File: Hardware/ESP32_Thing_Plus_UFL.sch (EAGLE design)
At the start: 50 parts, among them Q1 2.5A/30V, Q2 MBT3904DW1T1, U1 MCP73831, U3 AP2112K-3.3V, U4 CP210X, U5 ESP-WROOM-3232U-NARROW

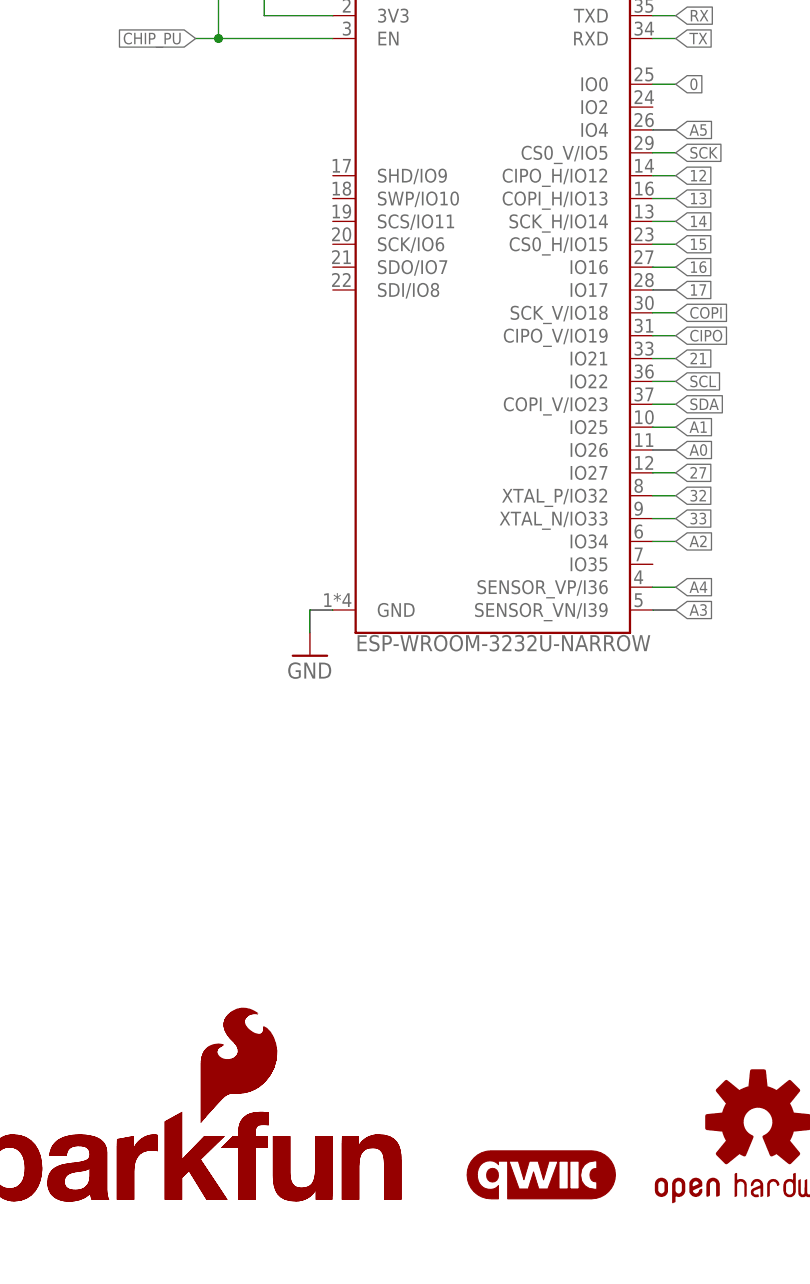
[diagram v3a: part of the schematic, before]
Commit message: aesthetic changes from post review review
-Change CIPO and COPI pin names in symbol to SDI/SDO
-Updated product name bottom silk to include "32"
-Removed extra top silk flame logo at bottom right (since we had room for the full name and flame logo at the top.
-changed silk names for DI/DO to SDI/SDO for more consitency in schematic/board naming.
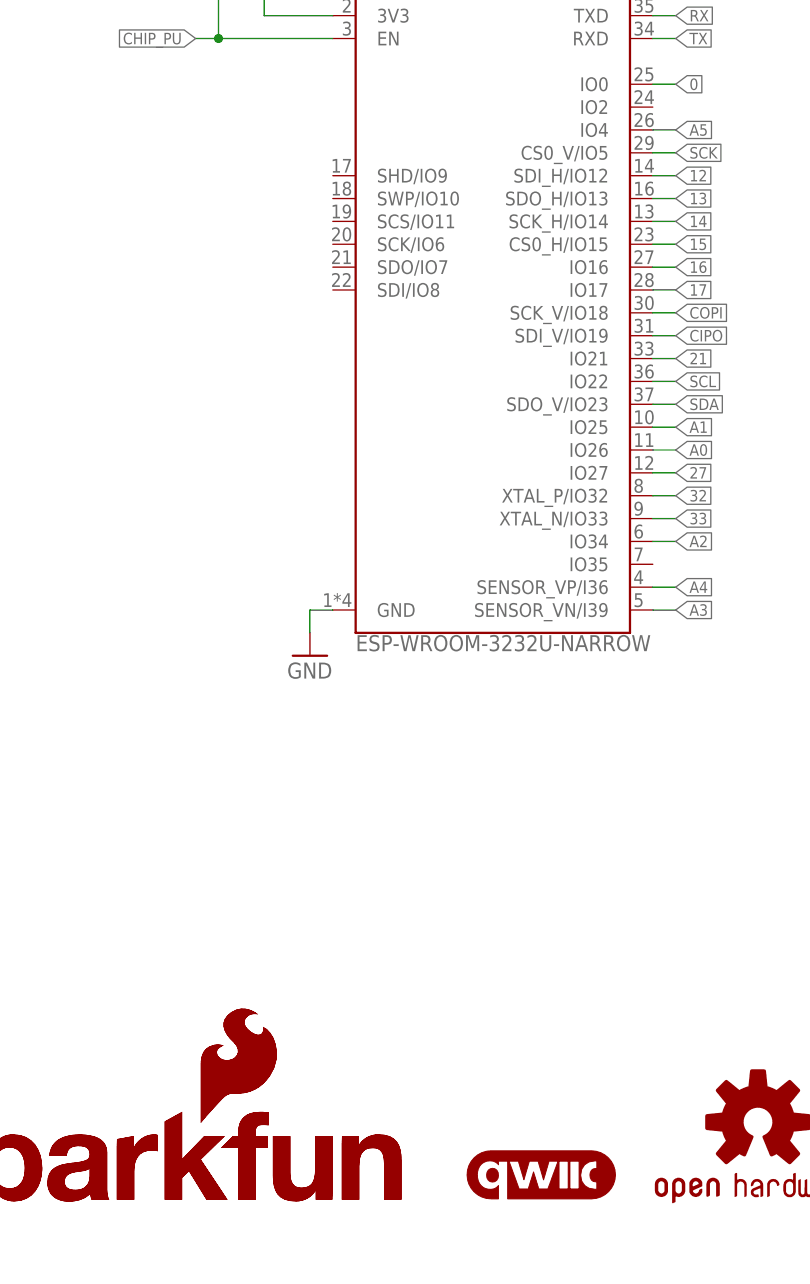
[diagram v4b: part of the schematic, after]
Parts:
- removed LOGO1: SFE_LOGO_FLAME.1_INCH, SparkFun-Aesthetics:SFE_LOGO_FLAME.1_INCH
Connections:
- net 12: now also U5.SDI_H/IO12; no longer U5.CIPO_H/IO12
- net 13: now also U5.SDO_H/IO13; no longer U5.COPI_H/IO13
- net CIPO: now also U5.SDI_V/IO19; no longer U5.CIPO_V/IO19
- net SDA: now also U5.SDO_V/IO23; no longer U5.COPI_V/IO23
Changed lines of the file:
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@@
 <grid distance="0.1" unitdist="inch" unit="inch" style="lines" multiple="1" display="no" altdistance="0.01" altunitdist="inch" altunit="inch"/>
 <layers>
-<layer number="1" name="Top" color="4" fill="1" visible="yes" active="no"/>
-<layer number="2" name="Route2" color="1" fill="3" visible="yes" active="no"/>
-<layer number="3" name="Route3" color="4" fill="3" visible="yes" active="no"/>
-<layer number="4" name="Route4" color="1" fill="4" visible="yes" active="no"/>
-<layer number="5" name="Route5" color="4" fill="4" visible="yes" active="no"/>
-<layer number="6" name="Route6" color="1" fill="8" visible="yes" active="no"/>
-<layer number="7" name="Route7" color="4" fill="8" visible="yes" active="no"/>
-<layer number="8" name="Route8" color="1" fill="2" visible="yes" active="no"/>
-<layer number="9" name="Route9" color="4" fill="2" visible="yes" active="no"/>
-<layer number="10" name="Route10" color="1" fill="7" visible="yes" active="no"/>
-<layer number="11" name="Route11" color="4" fill="7" visible="yes" active="no"/>
-<layer number="12" name="Route12" color="1" fill="5" visible="yes" active="no"/>
-<layer number="13" name="Route13" color="4" fill="5" visible="yes" active="no"/>
-<layer number="14" name="Route14" color="1" fill="6" visible="yes" active="no"/>
-<layer number="15" name="Route15" color="4" fill="6" visible="yes" active="no"/>
-<layer number="16" name="Bottom" color="1" fill="1" visible="yes" active="no"/>
-<layer number="17" name="Pads" color="2" fill="1" visible="yes" active="no"/>
-<layer number="18" name="Vias" color="2" fill="1" visible="yes" active="no"/>
-<layer number="19" name="Unrouted" color="6" fill="1" visible="yes" active="no"/>
-<layer number="20" name="Dimension" color="15" fill="1" visible="yes" active="no"/>
-<layer number="21" name="tPlace" color="16" fill="1" visible="yes" active="no"/>
-<layer number="22" name="bPlace" color="14" fill="1" visible="yes" active="no"/>
-<layer number="23" name="tOrigins" color="15" fill="1" visible="yes" active="no"/>
-<layer number="24" name="bOrigins" color="15" fill="1" visible="yes" active="no"/>
-<layer number="25" name="tNames" color="7" fill="1" visible="yes" active="no"/>
-<layer number="26" name="bNames" color="7" fill="1" visible="yes" active="no"/>
-<layer number="27" name="tValues" color="7" fill="1" visible="yes" active="no"/>
-<layer number="28" name="bValues" color="7" fill="1" visible="yes" active="no"/>
+<layer number="1" name="Top" color="4" fill="1" visible="no" active="no"/>
+<layer number="2" name="Route2" color="1" fill="3" visible="no" active="no"/>
+<layer number="3" name="Route3" color="4" fill="3" visible="no" active="no"/>
+<layer number="4" name="Route4" color="1" fill="4" visible="no" active="no"/>
+<layer number="5" name="Route5" color="4" fill="4" visible="no" active="no"/>
+<layer number="6" name="Route6" color="1" fill="8" visible="no" active="no"/>
+<layer number="7" name="Route7" color="4" fill="8" visible="no" active="no"/>
+<layer number="8" name="Route8" color="1" fill="2" visible="no" active="no"/>
+<layer number="9" name="Route9" color="4" fill="2" visible="no" active="no"/>
+<layer number="10" name="Route10" color="1" fill="7" visible="no" active="no"/>
+<layer number="11" name="Route11" color="4" fill="7" visible="no" active="no"/>
+<layer number="12" name="Route12" color="1" fill="5" visible="no" active="no"/>
+<layer number="13" name="Route13" color="4" fill="5" visible="no" active="no"/>
+<layer number="14" name="Route14" color="1" fill="6" visible="no" active="no"/>
+<layer number="15" name="Route15" color="4" fill="6" visible="no" active="no"/>
+<layer number="16" name="Bottom" color="1" fill="1" visible="no" active="no"/>
+<layer number="17" name="Pads" color="2" fill="1" visible="no" active="no"/>
+<layer number="18" name="Vias" color="2" fill="1" visible="no" active="no"/>
+<layer number="19" name="Unrouted" color="6" fill="1" visible="no" active="no"/>
+<layer number="20" name="Dimension" color="15" fill="1" visible="no" active="no"/>
+<layer number="21" name="tPlace" color="16" fill="1" visible="no" active="no"/>
+<layer number="22" name="bPlace" color="14" fill="1" visible="no" active="no"/>
+<layer number="23" name="tOrigins" color="15" fill="1" visible="no" active="no"/>
+<layer number="24" name="bOrigins" color="15" fill="1" visible="no" active="no"/>
+<layer number="25" name="tNames" color="7" fill="1" visible="no" active="no"/>
+<layer number="26" name="bNames" color="7" fill="1" visible="no" active="no"/>
+<layer number="27" name="tValues" color="7" fill="1" visible="no" active="no"/>
+<layer number="28" name="bValues" color="7" fill="1" visible="no" active="no"/>
 <layer number="29" name="tStop" color="7" fill="3" visible="no" active="no"/>
 <layer number="30" name="bStop" color="7" fill="6" visible="no" active="no"/>
@@
 <layer number="35" name="tGlue" color="7" fill="4" visible="no" active="no"/>
 <layer number="36" name="bGlue" color="7" fill="5" visible="no" active="no"/>
-<layer number="37" name="tTest" color="7" fill="1" visible="yes" active="no"/>
-<layer number="38" name="bTest" color="7" fill="1" visible="yes" active="no"/>
+<layer number="37" name="tTest" color="7" fill="1" visible="no" active="no"/>
+<layer number="38" name="bTest" color="7" fill="1" visible="no" active="no"/>
 <layer number="39" name="tKeepout" color="4" fill="11" visible="no" active="no"/>
 <layer number="40" name="bKeepout" color="1" fill="11" visible="no" active="no"/>
@@
 <layer number="44" name="Drills" color="7" fill="1" visible="no" active="no"/>
 <layer number="45" name="Holes" color="7" fill="1" visible="no" active="no"/>
-<layer number="46" name="Milling" color="3" fill="1" visible="yes" active="no"/>
-<layer number="47" name="Measures" color="7" fill="1" visible="yes" active="no"/>
-<layer number="48" name="Document" color="7" fill="1" visible="yes" active="no"/>
-<layer number="49" name="Reference" color="7" fill="1" visible="yes" active="no"/>
-<layer number="50" name="dxf" color="7" fill="1" visible="yes" active="no"/>
-<layer number="51" name="tDocu" color="6" fill="1" visible="yes" active="no"/>
-<layer number="52" name="bDocu" color="7" fill="1" visible="yes" active="no"/>
-<layer number="53" name="tGND_GNDA" color="7" fill="9" visible="yes" active="no"/>
-<layer number="54" name="bGND_GNDA" color="1" fill="9" visible="yes" active="no"/>
-<layer number="56" name="wert" color="7" fill="1" visible="yes" active="no"/>
-<layer number="57" name="tCAD" color="7" fill="1" visible="yes" active="no"/>
-<layer number="59" name="tCarbon" color="7" fill="1" visible="yes" active="no"/>
-<layer number="60" name="bCarbon" color="7" fill="1" visible="yes" active="no"/>
+<layer number="46" name="Milling" color="3" fill="1" visible="no" active="no"/>
+<layer number="47" name="Measures" color="7" fill="1" visible="no" active="no"/>
+<layer number="48" name="Document" color="7" fill="1" visible="no" active="no"/>
+<layer number="49" name="Reference" color="7" fill="1" visible="no" active="no"/>
+<layer number="50" name="dxf" color="7" fill="1" visible="no" active="no"/>
+<layer number="51" name="tDocu" color="6" fill="1" visible="no" active="no"/>
+<layer number="52" name="bDocu" color="7" fill="1" visible="no" active="no"/>
+<layer number="53" name="tGND_GNDA" color="7" fill="9" visible="no" active="no"/>
+<layer number="54" name="bGND_GNDA" color="1" fill="9" visible="no" active="no"/>
+<layer number="56" name="wert" color="7" fill="1" visible="no" active="no"/>
+<layer number="57" name="tCAD" color="7" fill="1" visible="no" active="no"/>
+<layer number="59" name="tCarbon" color="7" fill="1" visible="no" active="no"/>
+<layer number="60" name="bCarbon" color="7" fill="1" visible="no" active="no"/>
 <layer number="88" name="SimResults" color="9" fill="1" visible="yes" active="yes"/>
 <layer number="89" name="SimProbes" color="9" fill="1" visible="yes" active="yes"/>
@@
 <part name="GND5" library="SparkFun-Aesthetics" deviceset="GND" device=""/>
 <part name="R8" library="SparkFun-Resistors" deviceset="100KOHM" device="-0402T-1/16W-1%" value="100k"/>
-<part name="LOGO1" library="SparkFun-Aesthetics" deviceset="SFE_LOGO_FLAME" device=".1_INCH"/>
 <part name="LOGO3" library="SparkFun-Aesthetics" deviceset="SFE_LOGO_NAME_FLAME" device=".1_INCH"/>
 <part name="LOGO4" library="SparkFun-Aesthetics" deviceset="FOUR_LAYER_WARNING" device=""/>
@@
 <attribute name="VALUE" x="63.5" y="234.696" size="1.778" layer="96" font="vector" align="top-center"/>
 </instance>
-<instance part="LOGO1" gate="G$1" x="84.074" y="18.796" smashed="yes"/>
 <instance part="LOGO3" gate="G$1" x="51.562" y="6.096" smashed="yes"/>
 <instance part="LOGO4" gate="G$1" x="393.7" y="38.1" smashed="yes"/>
@@
 <wire x1="134.62" y1="106.68" x2="137.16" y2="106.68" width="0.1524" layer="91"/>
 <label x="137.16" y="106.68" size="1.27" layer="95" xref="yes"/>
-<pinref part="U5" gate="G$1" pin="CIPO_V/IO19"/>
+<pinref part="U5" gate="G$1" pin="SDI_V/IO19"/>
 </segment>
 </net>
@@
 <wire x1="134.62" y1="99.06" x2="137.16" y2="99.06" width="0.1524" layer="91"/>
 <label x="137.16" y="99.06" size="1.27" layer="95" xref="yes"/>
-<pinref part="U5" gate="G$1" pin="COPI_V/IO23"/>
+<pinref part="U5" gate="G$1" pin="SDO_V/IO23"/>
 </segment>
 </net>
@@
 <wire x1="134.62" y1="124.46" x2="137.16" y2="124.46" width="0.1524" layer="91"/>
 <label x="137.16" y="124.46" size="1.27" layer="95" xref="yes"/>
-<pinref part="U5" gate="G$1" pin="CIPO_H/IO12"/>
+<pinref part="U5" gate="G$1" pin="SDI_H/IO12"/>
 </segment>
 </net>
@@
 <wire x1="134.62" y1="121.92" x2="137.16" y2="121.92" width="0.1524" layer="91"/>
 <label x="137.16" y="121.92" size="1.27" layer="95" xref="yes"/>
-<pinref part="U5" gate="G$1" pin="COPI_H/IO13"/>
-</segment>
-</net>
+<pinref part="U5" gate="G$1" pin="SDO_H/IO13"/>
+</segment>
+</net>

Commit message: Run of checklist catches
-vector font in sch
-flag label on NET "0"
-changes top silk on RST pin to include active low marking
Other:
- moved on the sheet: TP1

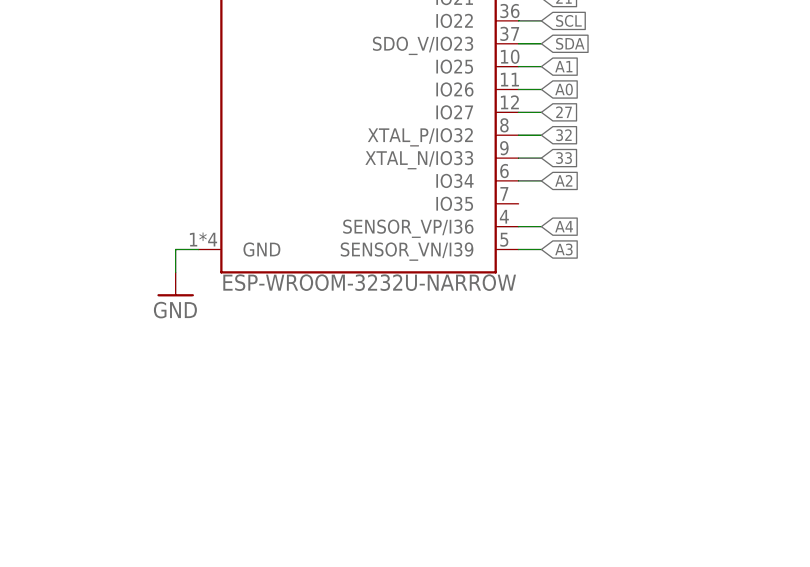
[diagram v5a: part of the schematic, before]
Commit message: changing library part names/descriptions to the 32EU
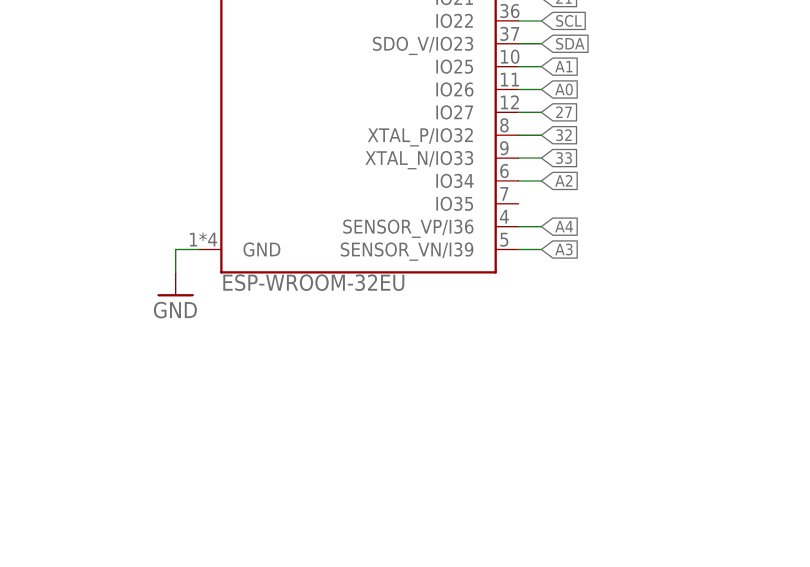
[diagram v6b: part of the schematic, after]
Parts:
- U5: value ESP-WROOM-3232U-NARROW -> ESP-WROOM-32EU
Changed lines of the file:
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@@
 <part name="H1" library="SparkFun-Hardware" deviceset="STAND-OFF" device="TIGHT"/>
 <part name="H2" library="SparkFun-Hardware" deviceset="STAND-OFF" device="TIGHT"/>
-<part name="U5" library="esp-wroom-32u" deviceset="ESP-WROOM-32" device="32U-NARROW"/>
+<part name="U5" library="esp-wroom-32u" deviceset="ESP-WROOM-32" device="32U-NARROW" value="ESP-WROOM-32EU"/>
 <part name="GND8" library="SparkFun-Aesthetics" deviceset="GND" device=""/>
 <part name="H3" library="SparkFun-Hardware" deviceset="STAND-OFF" device="TIGHT"/>

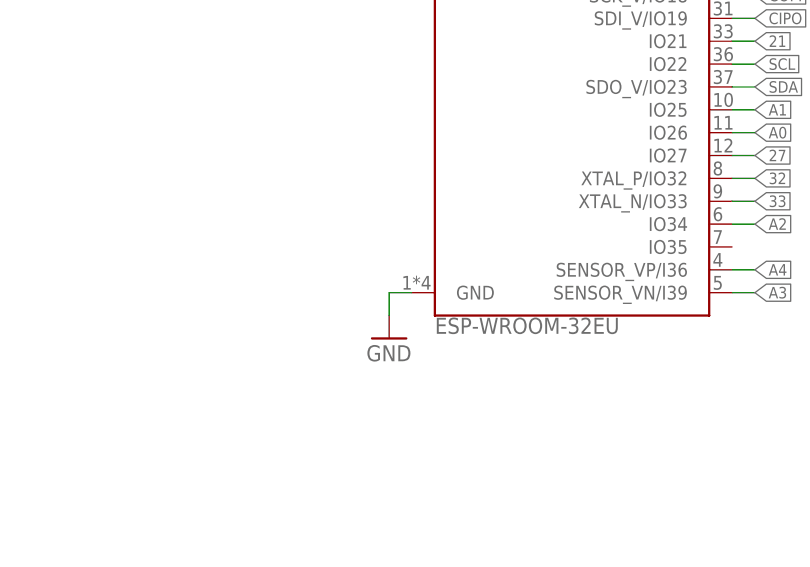
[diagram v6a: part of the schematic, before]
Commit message: updated ESP32EU footprint to match gnd pad array from datasheet
-also added gnd pours to top and bottom copper
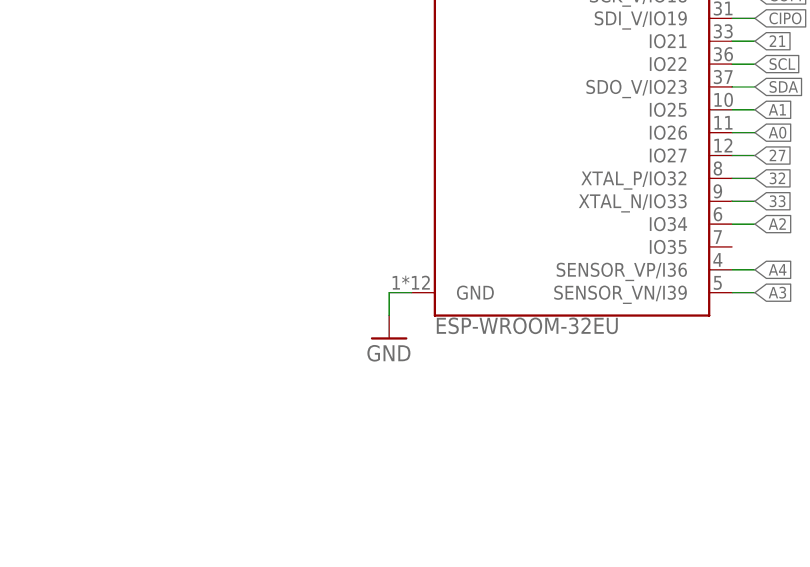
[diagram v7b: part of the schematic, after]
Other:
- moved on the sheet: U5
